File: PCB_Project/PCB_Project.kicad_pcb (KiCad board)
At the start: 2 copper layers, 3 parts, among them U5 TSR_1-2433, U6 TSR_1-24120

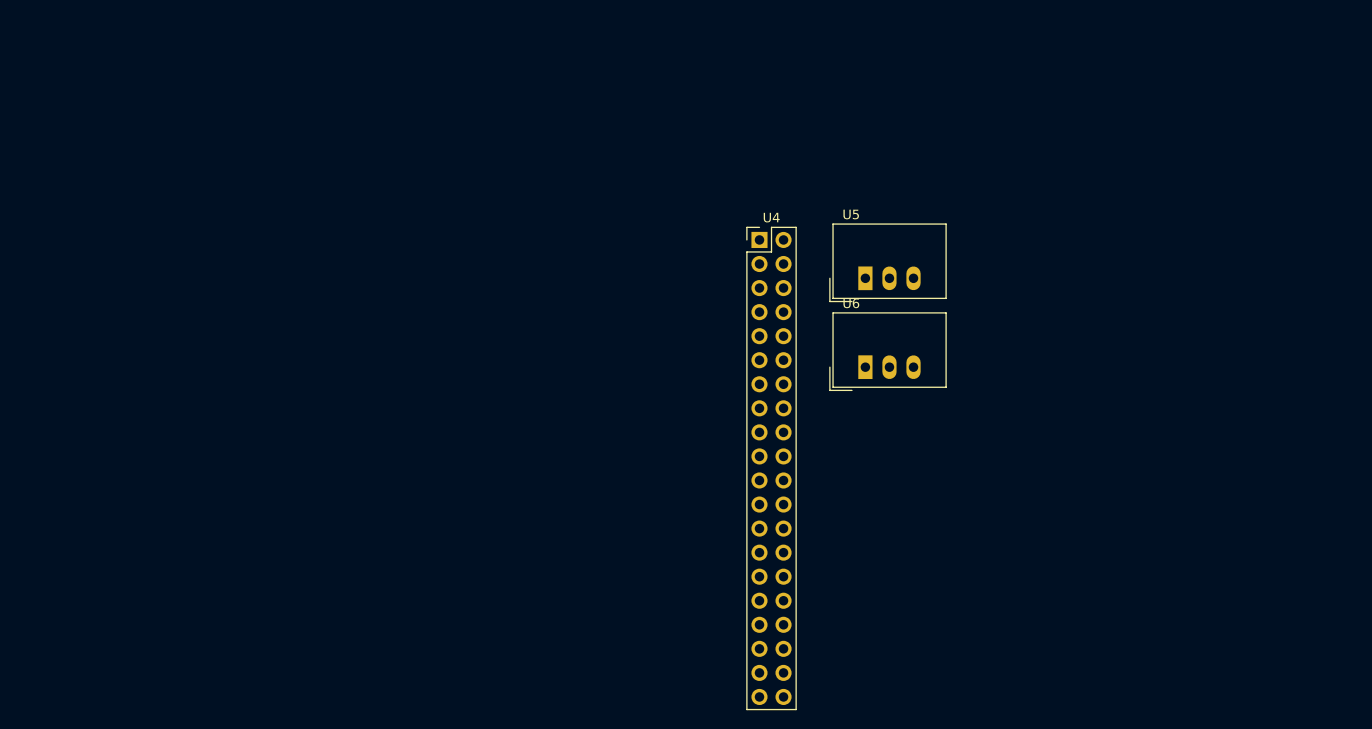
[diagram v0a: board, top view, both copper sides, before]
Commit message: 2 footprints left then can design
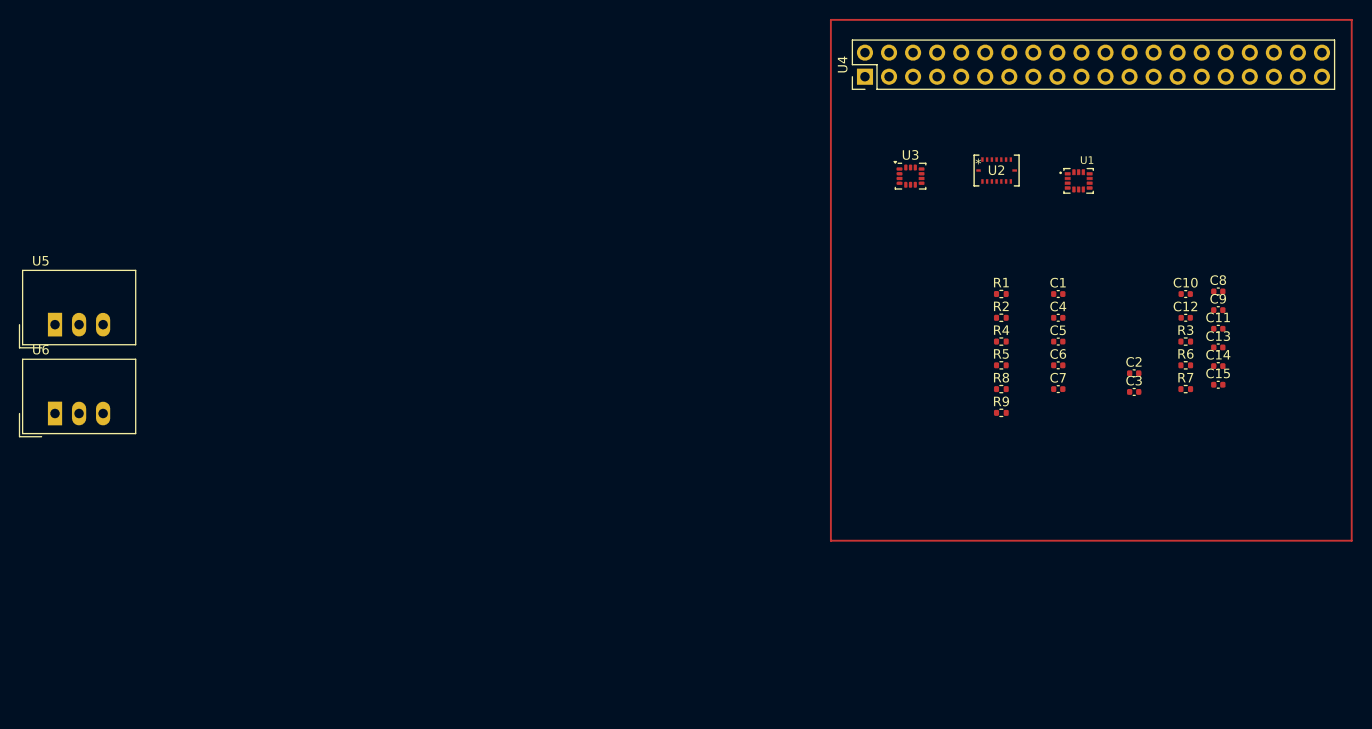
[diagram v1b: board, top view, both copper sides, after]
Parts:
- added C1: 10nF, Capacitor_SMD:C_0402_1005Metric, F.Cu at (137.5, 86.5)
- added C10: 100nF, Capacitor_SMD:C_0402_1005Metric, F.Cu at (151.0, 86.5)
- added C11: 1 µF, Capacitor_SMD:C_0402_1005Metric, F.Cu at (154.4, 90.1)
- added C12: 100nF, Capacitor_SMD:C_0402_1005Metric, F.Cu at (151.0, 89.0)
- added C13: 0.1µF, Capacitor_SMD:C_0402_1005Metric, F.Cu at (154.4, 92.1)
- added C14: 0.1µF, Capacitor_SMD:C_0402_1005Metric, F.Cu at (154.4, 94.1)
- added C15: 0.1µF, Capacitor_SMD:C_0402_1005Metric, F.Cu at (154.4, 96.0)
- added C2: 0.1uF, Capacitor_SMD:C_0402_1005Metric, F.Cu at (145.5, 94.8)
- added C3: 2.2uF, Capacitor_SMD:C_0402_1005Metric, F.Cu at (145.5, 96.8)
- added C4: 100nF, Capacitor_SMD:C_0402_1005Metric, F.Cu at (137.5, 89.0)
- added C5: 100nF, Capacitor_SMD:C_0402_1005Metric, F.Cu at (137.5, 91.5)
- added C6: 100nF, Capacitor_SMD:C_0402_1005Metric, F.Cu at (137.5, 94.0)
- added C7: 100nF, Capacitor_SMD:C_0402_1005Metric, F.Cu at (137.5, 96.5)
- added C8: 1µF, Capacitor_SMD:C_0402_1005Metric, F.Cu at (154.4, 86.2)
- added C9: 1µF, Capacitor_SMD:C_0402_1005Metric, F.Cu at (154.4, 88.2)
- added R1: 5k, Resistor_SMD:R_0402_1005Metric, F.Cu at (131.5, 86.5)
- added R2: 5k, Resistor_SMD:R_0402_1005Metric, F.Cu at (131.5, 89.0)
- added R3: 4.7k, Resistor_SMD:R_0402_1005Metric, F.Cu at (151.0, 91.5)
- added R4: 5k, Resistor_SMD:R_0402_1005Metric, F.Cu at (131.5, 91.5)
- added R5: 5k, Resistor_SMD:R_0402_1005Metric, F.Cu at (131.5, 94.0)
- added R6: 10K, Resistor_SMD:R_0402_1005Metric, F.Cu at (151.0, 94.0)
- added R7: 10K, Resistor_SMD:R_0402_1005Metric, F.Cu at (151.0, 96.5)
- added R8: 5k, Resistor_SMD:R_0402_1005Metric, F.Cu at (131.5, 96.5)
- added R9: 5k, Resistor_SMD:R_0402_1005Metric, F.Cu at (131.5, 99.0)
- added U1: ~, Sensor:PQFN50P250X300X97-14N, F.Cu at (139.7, 74.5)
- added U2: ~, Sensor:QFN_BMI085_BOS, F.Cu at (131.0, 73.4)
- added U3: ~, Package_LGA:LGA-14_3x2.5mm_P0.5mm_LayoutBorder3x4y, F.Cu at (121.9, 74.0)
- moved U5 85.7 mm to (31.6, 89.7)
- moved U6 85.7 mm to (31.6, 99.1)
- moved U4 20.5 mm to (117.1, 63.5), turned to 90 degrees

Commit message: pcb work
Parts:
- added J1: Batt_Connector, Connector_JST:JST_PH_B2B-PH-K_1x02_P2.00mm_Vertical, F.Cu at (157.8, 76.0)
- added J3: Motor_Connector, Connector_JST:JST_PH_B2B-PH-K_1x02_P2.00mm_Vertical, F.Cu at (119.8, 85.1)
- added J4: Motor_Connector, Connector_JST:JST_PH_B2B-PH-K_1x02_P2.00mm_Vertical, F.Cu at (119.8, 91.7)
- added J5: Motor_Connector, Connector_JST:JST_PH_B2B-PH-K_1x02_P2.00mm_Vertical, F.Cu at (119.8, 98.2)
- added J6: Motor_Connector, Connector_JST:JST_PH_B2B-PH-K_1x02_P2.00mm_Vertical, F.Cu at (119.8, 104.8)
- added U10: ~, Sensor:WSON8_DEH_TEX, F.Cu at (157.4, 109.1)
- added U11: ~, Sensor:SOIC127P600X175-8N_ADT7410TRZ-REEL, F.Cu at (159.7, 103.7)
- added U12: ~, Package_LGA:LGA-12_2x2mm_P0.5mm, F.Cu at (166.0, 102.4)
- added U9: ~, Sensor:XDCR_SGP41-D-R4, F.Cu at (162.6, 109.0)

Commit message: need to fix the one damn footprint
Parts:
- removed C6, C7: 100nF, Capacitor_SMD:C_0402_1005Metric
- removed J1: Batt_Connector, Connector_JST:JST_PH_B2B-PH-K_1x02_P2.00mm_Vertical
- removed U3: ~, Package_LGA:LGA-14_3x2.5mm_P0.5mm_LayoutBorder3x4y
- removed U5: TSR_1-2433, Converter_DCDC:Converter_DCDC_TRACO_TSR-1_THT
- removed U6: TSR_1-24120, Converter_DCDC:Converter_DCDC_TRACO_TSR-1_THT
- added J2: ZE27-O3, Connector_JST:JST_EH_B5B-EH-A_1x05_P2.50mm_Vertical, F.Cu at (75.5, 63.0)
- added U8: ~, Sensor:HNNJ footprint, F.Cu at (154.8, 109.2)
- U1: footprint Sensor:PQFN50P250X300X97-14N -> Package_LGA:LGA-24L_3x3.5mm_P0.43mm
- moved U10 19.1 mm to (156.4, 90.1)
- moved U11 19.1 mm to (158.7, 84.7)
- moved U9 19.1 mm to (161.6, 89.9)
- moved U12 19.1 mm to (165.0, 83.4)
- moved C10 11.7 mm to (146.7, 75.5)
- moved C11 11.7 mm to (150.2, 79.2)
- moved C13 11.7 mm to (150.2, 81.1)
- moved C14 11.7 mm to (150.2, 83.1)
- moved C15 11.7 mm to (150.2, 85.1)
- moved C8 11.7 mm to (150.2, 75.2)
- moved C9 11.7 mm to (150.2, 77.2)
- moved R3 11.7 mm to (146.7, 80.5)
- moved R6 11.7 mm to (146.7, 83.0)
- moved C12 11.7 mm to (146.7, 78.0)
- moved R7 11.7 mm to (146.7, 85.5)
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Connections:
- U10 pad 9: (no net) -> GND
- U4 pad 11: unconnected-(U4-GPIO_17-Pad11) -> CSB_Gryo_BMI088
- U4 pad 12: (no net) -> nCS_2
- U4 pad 19: unconnected-(U4-GPIO_10_MOSI-Pad19) -> SDI_1
- U4 pad 21: unconnected-(U4-GPIO_9_MISO-Pad21) -> SDO_1
- U4 pad 23: unconnected-(U4-GPIO_11_SCLK-Pad23) -> SCK_1
- U4 pad 24: CSB_Gryo_BMI088 -> unconnected-(U4-GPIO_8-Pad24)
- U4 pad 35: unconnected-(U4-GPIO_19_PCM_FS-Pad35) -> SDO_2
- U4 pad 38: unconnected-(U4-GPIO_20_(PCM_DIN)-Pad38) -> SDI_2
- U4 pad 40: unconnected-(U4-GPIO_21_(PCM_DOUT)-Pad40) -> SCLK_2
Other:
- board outline added: 55 x 55 mm

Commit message: second gerber files
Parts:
- removed C1: 10nF, Capacitor_SMD:C_0402_1005Metric
- removed C2: 0.1uF, Capacitor_SMD:C_0402_1005Metric
- removed C3: 2.2uF, Capacitor_SMD:C_0402_1005Metric
- removed R6, R7: 10K, Resistor_SMD:R_0402_1005Metric
- removed U1: ~, Package_LGA:LGA-24L_3x3.5mm_P0.43mm
- U4: footprint Connector_PinHeader_2.54mm:PinHeader_2x20_P2.54mm_Vertical -> Connector_PinSocket_2.54mm:PinSocket_2x20_P2.54mm_Vertical; moved to B.Cu
- moved J2 90.0 mm to (153.5, 108.0)
- moved U12 46.0 mm to (119.6, 75.6)
- moved R9 32.6 mm to (147.2, 67.0)
- moved R8 31.9 mm to (149.7, 67.0)
- moved J3 31.8 mm to (126.2, 107.5)
- moved C10 30.4 mm to (116.3, 76.3), turned to 180 degrees
- moved C11 30.4 mm to (119.8, 79.4)
- moved J5 30.2 mm to (143.0, 107.5)
- moved J4 29.1 mm to (134.5, 107.5)
- moved U9 29.0 mm to (137.3, 74.0)
- moved C12 26.9 mm to (119.8, 78.0)
- moved R1 26.5 mm to (152.2, 67.0)
- moved R5 25.1 mm to (121.8, 67.0)
- moved R4 24.0 mm to (119.0, 67.0)
- moved U10 19.9 mm to (136.8, 86.5)
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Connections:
- J2 pad 2: unconnected-(J2-UART_TXD_(Out)-Pad2) -> Pi_TX
- J2 pad 3: unconnected-(J2-UART_RX_(In)-Pad3) -> Pi_RX
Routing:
- net +3V3: track 0.00 -> 188.2 mm, vias 0 -> 2
- net I2C_SCL_M: track 0.00 -> 82.4 mm, vias 0 -> 2
- net I2C_SDA_M: track 0.00 -> 79.8 mm, vias 0 -> 2
- net +5V: track 0.00 -> 64.3 mm
- net I2C_SDA_1: track 0.00 -> 64.1 mm, vias 0 -> 3
- net I2C_SCL_1: track 0.00 -> 64.0 mm, vias 0 -> 3
- net Pi_TX: track 0.00 -> 61.7 mm
- net Pi_RX: track 0.00 -> 61.5 mm
- net I2C_SDA_2: track 0.00 -> 60.5 mm, vias 0 -> 7
- net I2C_SCL_2: track 0.00 -> 57.0 mm
- net CSB_Accel_BMI088: track 0.00 -> 54.8 mm, vias 0 -> 1
- net SDO_1: track 0.00 -> 46.1 mm
- net SCK_1: track 0.00 -> 39.8 mm
- net SDI_1: track 0.00 -> 36.0 mm, vias 0 -> 1
- net CSB_Gryo_BMI088: track 0.00 -> 29.5 mm
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- added copper zone on F.Cu, net GND

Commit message: everything is now hooked up
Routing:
- net GND: track 12.1 -> 27.5 mm, vias 2 -> 45
- net +3V3: track 188.2 -> 191.5 mm
- net I2C_SDA_1: track 64.1 -> 63.5 mm
- net I2C_SDA_2: track 60.5 -> 60.0 mm
- added copper zone on B.Cu, net GND

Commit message: Rerouted and Cleaned up Board
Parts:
- R3: value 4.7k -> 4.7
- moved R2 0.75 mm to (124.5, 67.0), turned to 90 degrees
- moved R4 0.50 mm to (119.5, 67.0), turned to 90 degrees
- moved R8 0.26 mm to (150.0, 67.0), turned to 90 degrees
- moved R1 0.25 mm to (152.5, 67.0), turned to 90 degrees
- moved R5 0.25 mm to (122.0, 67.0), turned to 90 degrees
- moved R9 0.25 mm to (147.5, 67.0), turned to 90 degrees
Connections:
- J2 pad 2: Pi_TX -> Pi_RX
- J2 pad 3: Pi_RX -> Pi_TX
- R4 pad 2: I2C_SCL_1 -> I2C_SDA_1
- R5 pad 2: I2C_SDA_1 -> I2C_SCL_1
- U4 pad 3: I2C_SCL_1 -> I2C_SDA_1
- U4 pad 5: I2C_SDA_1 -> I2C_SCL_1
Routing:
- net GND: track 27.5 -> 15.4 mm, vias 45 -> 46
- net +3V3: track 191.5 -> 181.4 mm, vias 2 -> 1
- net Pi_TX: track 61.7 -> 66.0 mm
- net I2C_SCL_2: track 57.0 -> 55.7 mm
- net I2C_SDA_2: track 60.0 -> 58.9 mm
- net Pi_RX: track 61.5 -> 60.7 mm
- net I2C_SCL_1: track 64.0 -> 64.8 mm
- net I2C_SDA_M: track 79.8 -> 80.5 mm
- net I2C_SDA_1: track 63.5 -> 63.0 mm

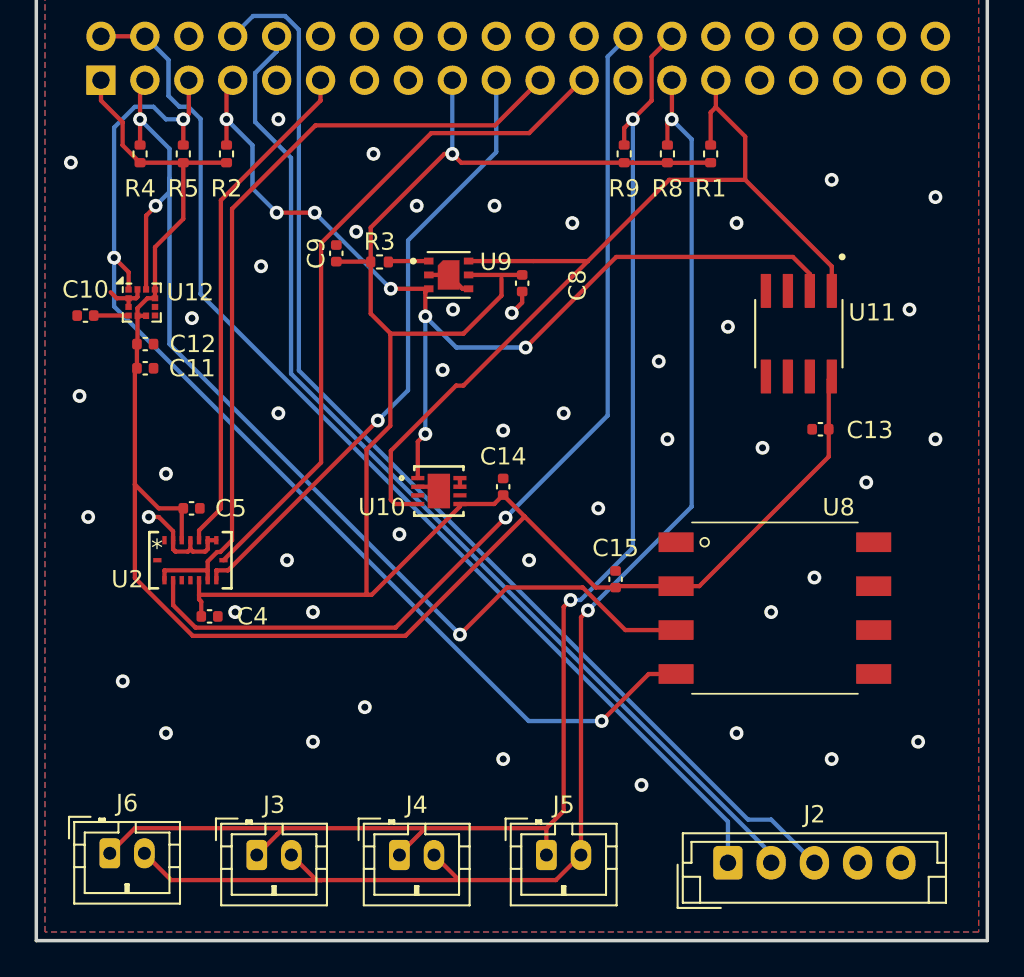
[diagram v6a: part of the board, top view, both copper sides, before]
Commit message: level shifters added to PCB
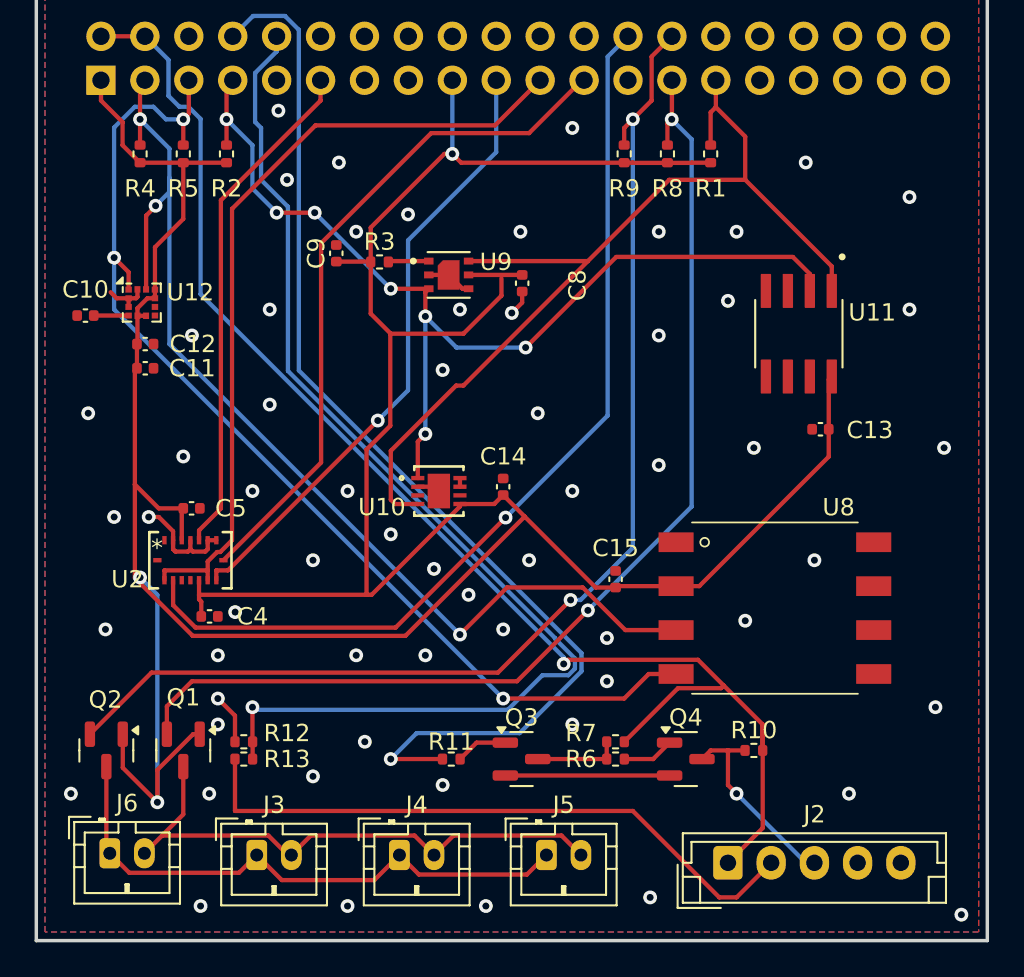
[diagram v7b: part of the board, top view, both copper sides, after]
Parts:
- added Q1: BSS138, Package_TO_SOT_SMD:SOT-23, F.Cu at (122.0, 101.5)
- added Q2: BSS138, Package_TO_SOT_SMD:SOT-23, F.Cu at (117.5, 101.5)
- added Q3: MMBT2222A, Package_TO_SOT_SMD:SOT-23, F.Cu at (141.6, 102.0)
- added Q4: MMBT2222A, Package_TO_SOT_SMD:SOT-23, F.Cu at (151.1, 102.0)
- added R10: 1k, Resistor_SMD:R_0402_1005Metric, F.Cu at (155.0, 101.5)
- added R11: 1k, Resistor_SMD:R_0402_1005Metric, F.Cu at (137.5, 102.0)
- added R12: 2k, Resistor_SMD:R_0402_1005Metric, F.Cu at (125.5, 101.0)
- added R13: 1k, Resistor_SMD:R_0402_1005Metric, F.Cu at (125.5, 102.0)
- added R6: 1k, Resistor_SMD:R_0402_1005Metric, F.Cu at (147.0, 102.0)
- added R7: 1k, Resistor_SMD:R_0402_1005Metric, F.Cu at (147.0, 101.0)
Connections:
- J2 pad 2: Pi_RX -> Pi_RX_5V
- J2 pad 3: Pi_TX -> Pi_TX_5V
- J3 pad 1: I2C_SCL_M -> I2C_SCL_M_5V
- J3 pad 2: I2C_SDA_M -> I2C_SDA_M_5V
- J4 pad 1: I2C_SCL_M -> I2C_SCL_M_5V
- J4 pad 2: I2C_SDA_M -> I2C_SDA_M_5V
- J5 pad 1: I2C_SCL_M -> I2C_SCL_M_5V
- J5 pad 2: I2C_SDA_M -> I2C_SDA_M_5V
- J6 pad 1: I2C_SCL_M -> I2C_SCL_M_5V
- J6 pad 2: I2C_SDA_M -> I2C_SDA_M_5V
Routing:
- net Pi_RX_5V: track 0.00 -> 36.9 mm
- net I2C_SCL_M_5V: track 0.00 -> 33.4 mm
- net I2C_SDA_M_5V: track 0.00 -> 32.5 mm
- net +3V3: track 181.4 -> 204.8 mm, vias 1 -> 3
- net I2C_SDA_M: track 80.5 -> 63.5 mm
- net +5V: track 64.6 -> 79.8 mm, vias 0 -> 1
- net I2C_SCL_M: track 82.6 -> 68.1 mm
- net GND: track 15.4 -> 27.9 mm, vias 46 -> 61
- net Pi_TX_5V: track 0.00 -> 11.6 mm, vias 0 -> 1
- net Pi_RX: track 60.7 -> 67.5 mm, vias 0 -> 1
- net Net-(Q3-C): track 0.00 -> 4.99 mm
- net Net-(Q4-B): track 0.00 -> 3.01 mm
- net Net-(Q3-B): track 0.00 -> 3.01 mm
- net Pi_TX: track 66.0 -> 64.6 mm, vias 0 -> 1
- net I2C_SCL_1: track 64.8 -> 63.8 mm

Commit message: soldering it to the board
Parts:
- J2: footprint Connector_JST:JST_EH_B5B-EH-A_1x05_P2.50mm_Vertical -> Connector_PinHeader_2.00mm:PinHeader_1x05_P2.00mm_Vertical
- moved J2 10.0 mm to (163.5, 107.5), turned to -90 degrees
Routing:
- net Pi_RX_5V: track 36.9 -> 40.5 mm
- net +5V: track 79.8 -> 81.4 mm
- net Pi_TX_5V: track 11.6 -> 12.4 mm
- net GND: vias 61 -> 66
